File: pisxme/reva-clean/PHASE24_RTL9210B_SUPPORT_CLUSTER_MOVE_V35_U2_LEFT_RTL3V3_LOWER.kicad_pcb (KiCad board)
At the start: 6 copper layers, 80 x 45 mm, 12 parts, among them J1 M.2 Socket 3 M-key 2280, U1 RTL9210B-CG, U2 W25Q128_SPI_FLASH, Y1 XTAL_25MHz

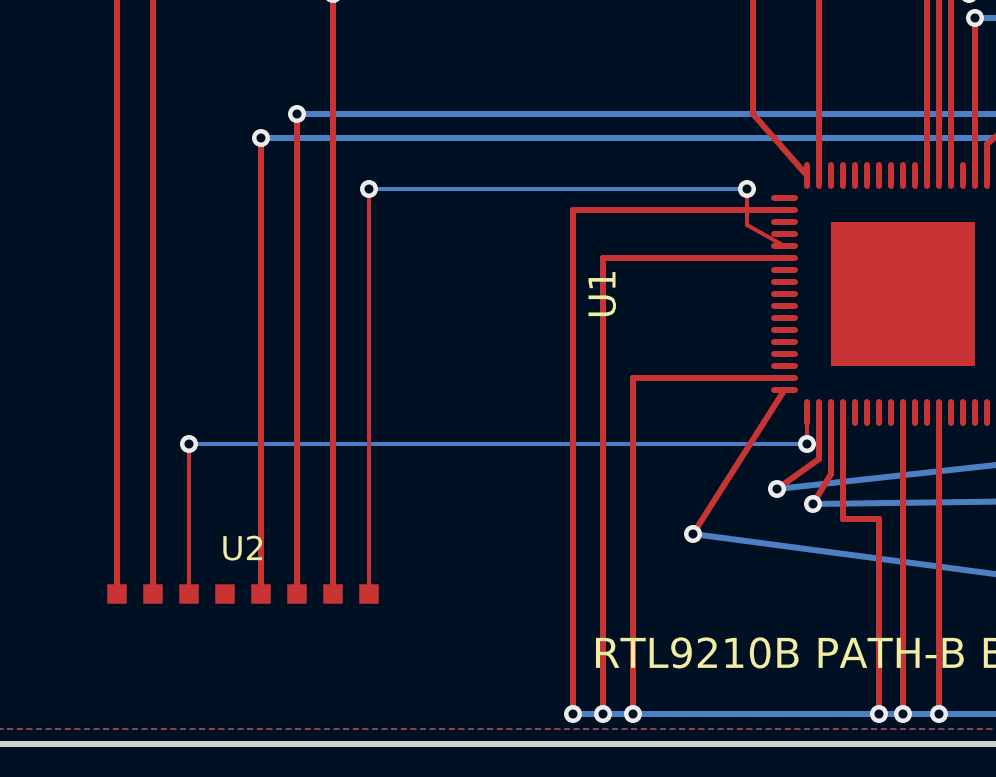
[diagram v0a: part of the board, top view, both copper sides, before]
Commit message: Record RTL9210B lower 3V3 field trials
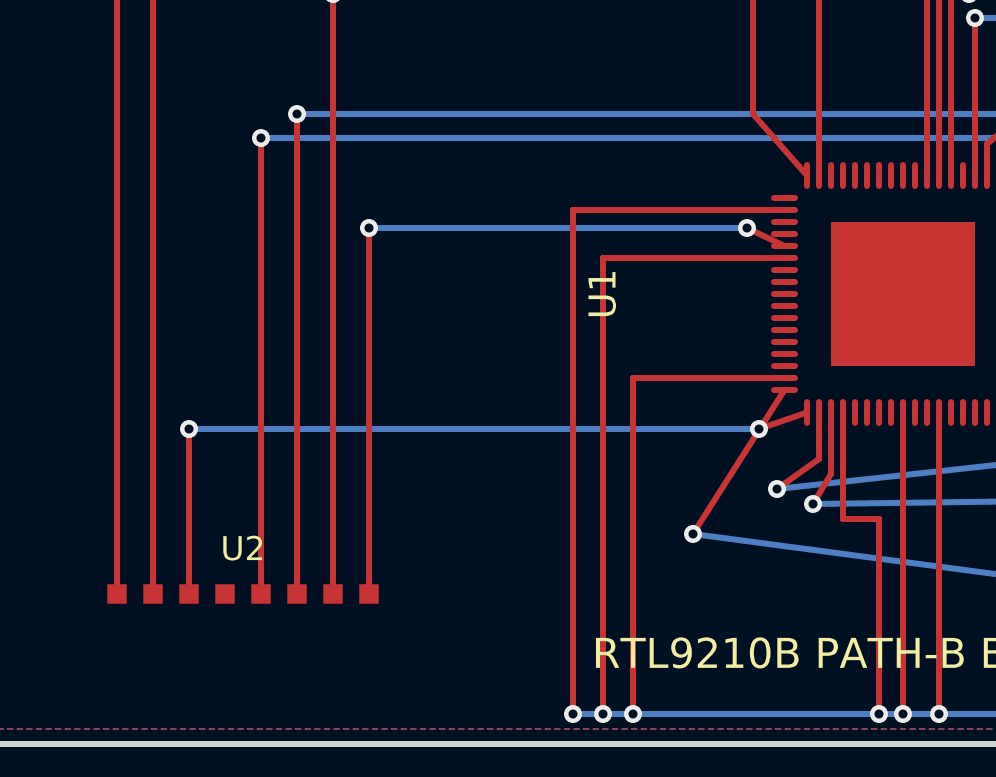
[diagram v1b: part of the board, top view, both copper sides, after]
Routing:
- net RTL_3V3: track 122.1 -> 119.1 mm
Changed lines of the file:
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@@
 	)
 	(segment
-		(start 94.8 73.95)
-		(end 94.8 75)
-		(width 0.13208)
+		(start 74.2 74.5)
+		(end 74.2 80)
+		(width 0.2)
 		(layer "F.Cu")
 		(net "RTL_3V3")
@@
 	)
 	(segment
-		(start 74.2 75)
-		(end 74.2 80)
-		(width 0.13208)
+		(start 94.05 68.4)
+		(end 92.8 67.8)
+		(width 0.2)
 		(layer "F.Cu")
 		(net "RTL_3V3")
@@
 		(end 100.4 60.8)
 		(width 0.2)
-		(layer "F.Cu")
-		(net "RTL_3V3")
-	)
-	(segment
-		(start 80.2 66.5)
-		(end 80.2 80)
-		(width 0.13208)
 		(layer "F.Cu")
 		(net "RTL_3V3")
@@
 	)
 	(segment
-		(start 94.05 68.4)
-		(end 92.8 67.7)
-		(width 0.13208)
+		(start 94.8 73.95)
+		(end 93.2 74.5)
+		(width 0.2)
 		(layer "F.Cu")
 		(net "RTL_3V3")
@@
 	)
 	(segment
-		(start 92.8 67.7)
-		(end 92.8 66.5)
-		(width 0.13208)
+		(start 80.2 67.8)
+		(end 80.2 80)
+		(width 0.2)
 		(layer "F.Cu")
 		(net "RTL_3V3")
@@
 	)
 	(via
-		(at 80.2 66.5)
+		(at 92.8 67.8)
 		(size 0.6)
 		(drill 0.3)
@@
 	)
 	(via
-		(at 92.8 66.5)
-		(size 0.6)
-		(drill 0.3)
-		(layers "F.Cu" "B.Cu")
-		(net "RTL_3V3")
-	)
-	(via
-		(at 94.8 75)
+		(at 80.2 67.8)
 		(size 0.6)
 		(drill 0.3)
@@
 	)
 	(via
-		(at 74.2 75)
+		(at 110 68.5)
 		(size 0.6)
 		(drill 0.3)
@@
 	)
 	(via
-		(at 110 68.5)
+		(at 74.2 74.5)
+		(size 0.6)
+		(drill 0.3)
+		(layers "F.Cu" "B.Cu")
+		(net "RTL_3V3")
+	)
+	(via
+		(at 93.2 74.5)
 		(size 0.6)
 		(drill 0.3)
@@
 	)
 	(segment
-		(start 94.8 75)
-		(end 74.2 75)
-		(width 0.13208)
+		(start 92.8 67.8)
+		(end 80.2 67.8)
+		(width 0.2)
 		(layer "B.Cu")
 		(net "RTL_3V3")
@@
 	)
 	(segment
+		(start 93.2 74.5)
+		(end 74.2 74.5)
+		(width 0.2)
+		(layer "B.Cu")
+		(net "RTL_3V3")
+	)
+	(segment
 		(start 100.4 60.8)
 		(end 110 60.8)
@@
 		(layer "B.Cu")
 		(net "RTL_3V3")
-	)
-	(segment
-		(start 92.8 66.5)
-		(end 80.2 66.5)
-		(width 0.13208)
-		(layer "B.Cu")
-		(net "RTL_3V3")
